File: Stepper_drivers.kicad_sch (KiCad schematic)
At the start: 9 parts, among them J6 ${STEPGEN_CH1_NAME}_STEP_AND_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, J7 ${STEPGEN_CH2_NAME}_STEP_AND_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, U5 ADuM1200AR, U6 ADuM1200AR, U7 HT26LS31ARZ

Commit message: Fixes to screw terminal footprints, updated BOM and included in project folder
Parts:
- J6, J7: footprint OSTVTerminalBlocks:Conn01x06 -> EBWA_06_A:CONN_EBWA-06-A_ADM
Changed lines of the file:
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@@
 				)
 				(path "/5473abc6-7b93-43cc-a401-f691c4d7d7cf/de6abc2f-b4f3-405f-80dc-20e6ec6edfe3"
-					(reference "#PWR0143")
-					(unit 1)
-				)
-				(path "/5473abc6-7b93-43cc-a401-f691c4d7d7cf/ee859447-e27b-4f56-862a-3601314a5b43"
-					(reference "#PWR0143")
+					(reference "#PWR0142")
+					(unit 1)
+				)
+				(path "/5473abc6-7b93-43cc-a401-f691c4d7d7cf/ee859447-e27b-4f56-862a-3601314a5b43"
+					(reference "#PWR0140")
 					(unit 1)
 				)
@@
 			)
 		)
-		(property "Footprint" "OSTVTerminalBlocks:Conn01x06"
+		(property "Footprint" "EBWA_06_A:CONN_EBWA-06-A_ADM"
 			(at 200.66 80.01 0)
 			(effects
@@
 			)
 		)
-		(property "Footprint" "OSTVTerminalBlocks:Conn01x06"
+		(property "Footprint" "EBWA_06_A:CONN_EBWA-06-A_ADM"
 			(at 200.66 105.41 0)
 			(effects

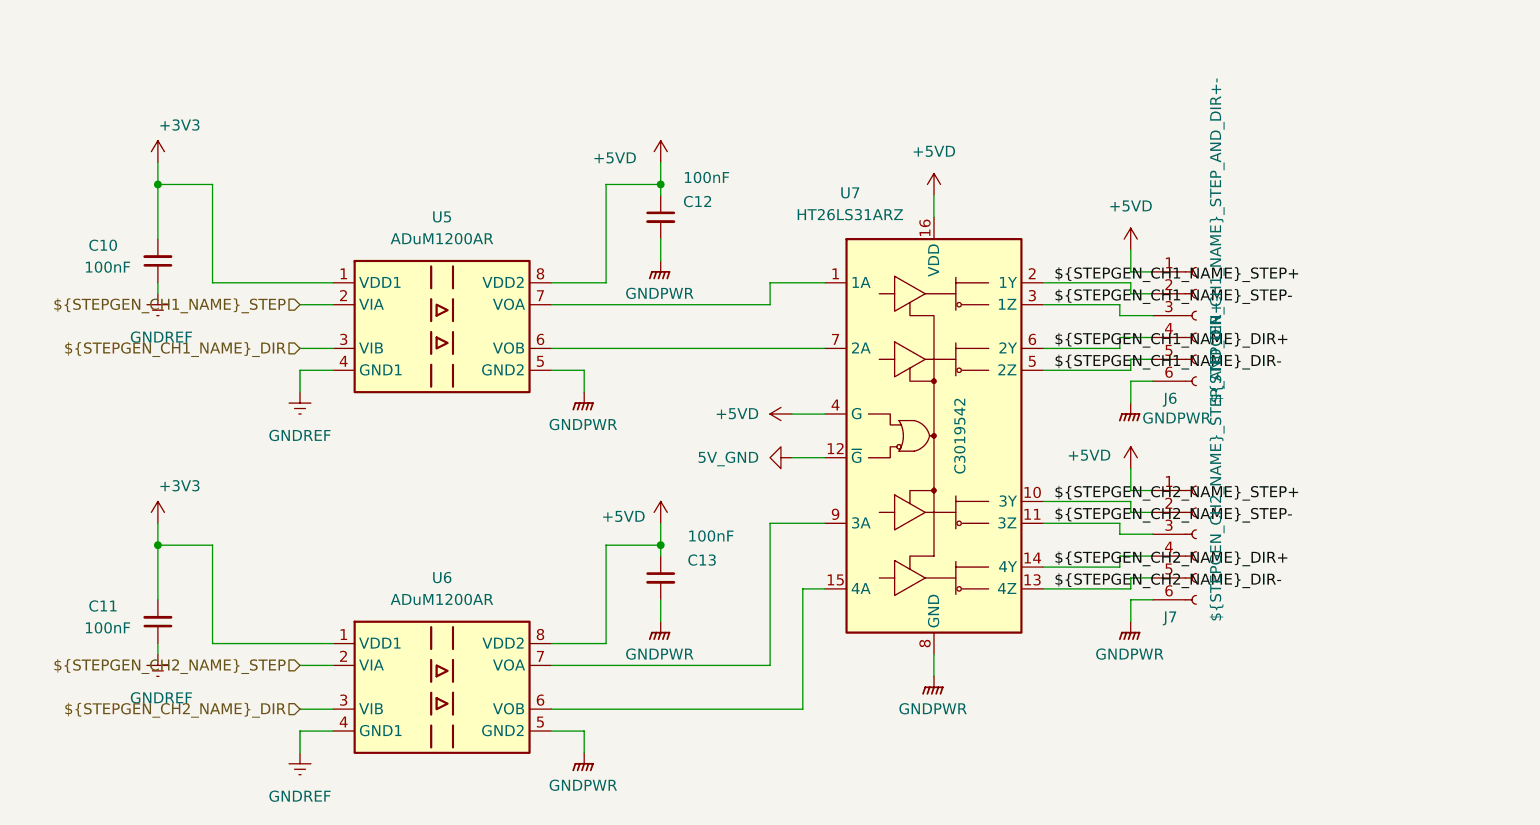
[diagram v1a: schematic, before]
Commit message: updates to read me, marked V1 parts inactive and made start on board layout for initial test board. fixes to BOM to suit
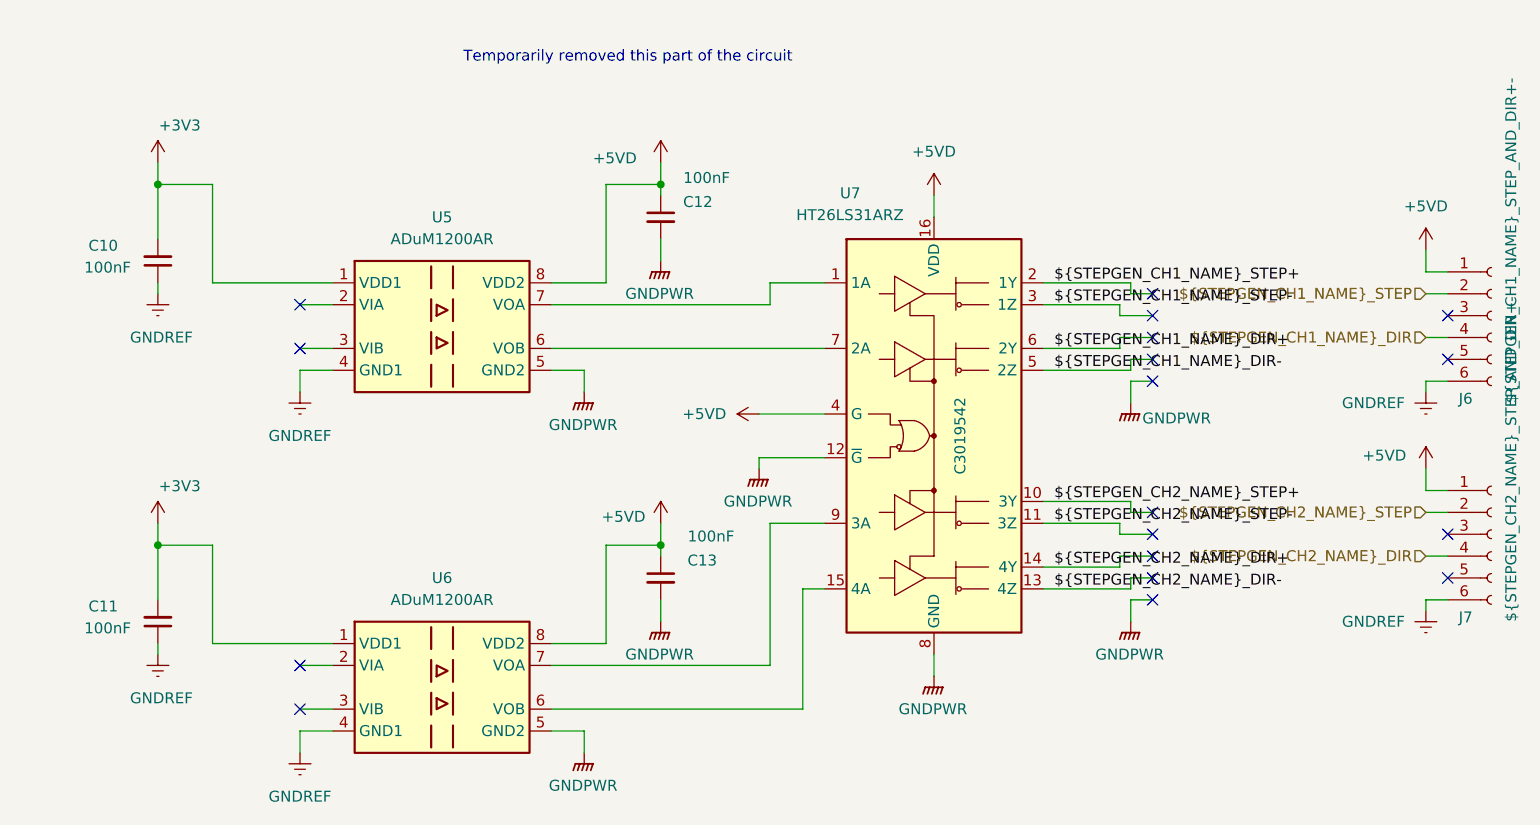
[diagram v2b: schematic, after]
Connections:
- net 5V_GND is gone; now on net GNDPWR: U7.12 (~{G})
- net ${STEPGEN_CH1_NAME}_DIR: now also J6.4 (Pin_4); no longer U5.3 (VIB)
- net ${STEPGEN_CH1_NAME}_DIR+: no longer J6.4 (Pin_4)
- net ${STEPGEN_CH1_NAME}_DIR-: no longer J6.5 (Pin_5)
- net ${STEPGEN_CH1_NAME}_STEP: now also J6.2 (Pin_2); no longer U5.2 (VIA)
- net ${STEPGEN_CH1_NAME}_STEP+: no longer J6.2 (Pin_2)
- net ${STEPGEN_CH1_NAME}_STEP-: no longer J6.3 (Pin_3)
- net ${STEPGEN_CH2_NAME}_DIR: now also J7.4 (Pin_4); no longer U6.3 (VIB)
- net ${STEPGEN_CH2_NAME}_DIR+: no longer J7.4 (Pin_4)
- net ${STEPGEN_CH2_NAME}_DIR-: no longer J7.5 (Pin_5)
- net ${STEPGEN_CH2_NAME}_STEP: now also J7.2 (Pin_2); no longer U6.2 (VIA)
- net ${STEPGEN_CH2_NAME}_STEP+: no longer J7.2 (Pin_2)
- net ${STEPGEN_CH2_NAME}_STEP-: no longer J7.3 (Pin_3)
- net GNDPWR: no longer J6.6 (Pin_6), J7.6 (Pin_6)
- net GNDREF: now also J6.6 (Pin_6), J7.6 (Pin_6)
- no-connect marks 0 -> 18
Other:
- note added: "Temporarily removed this part of the circuit"
- moved on the sheet: J6, J7

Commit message: New optocoupler part choice, removed digikey BOM as have started inputting them into symbol fields. Re-enabled all disabled parts for now and will re-design power supplies soon.
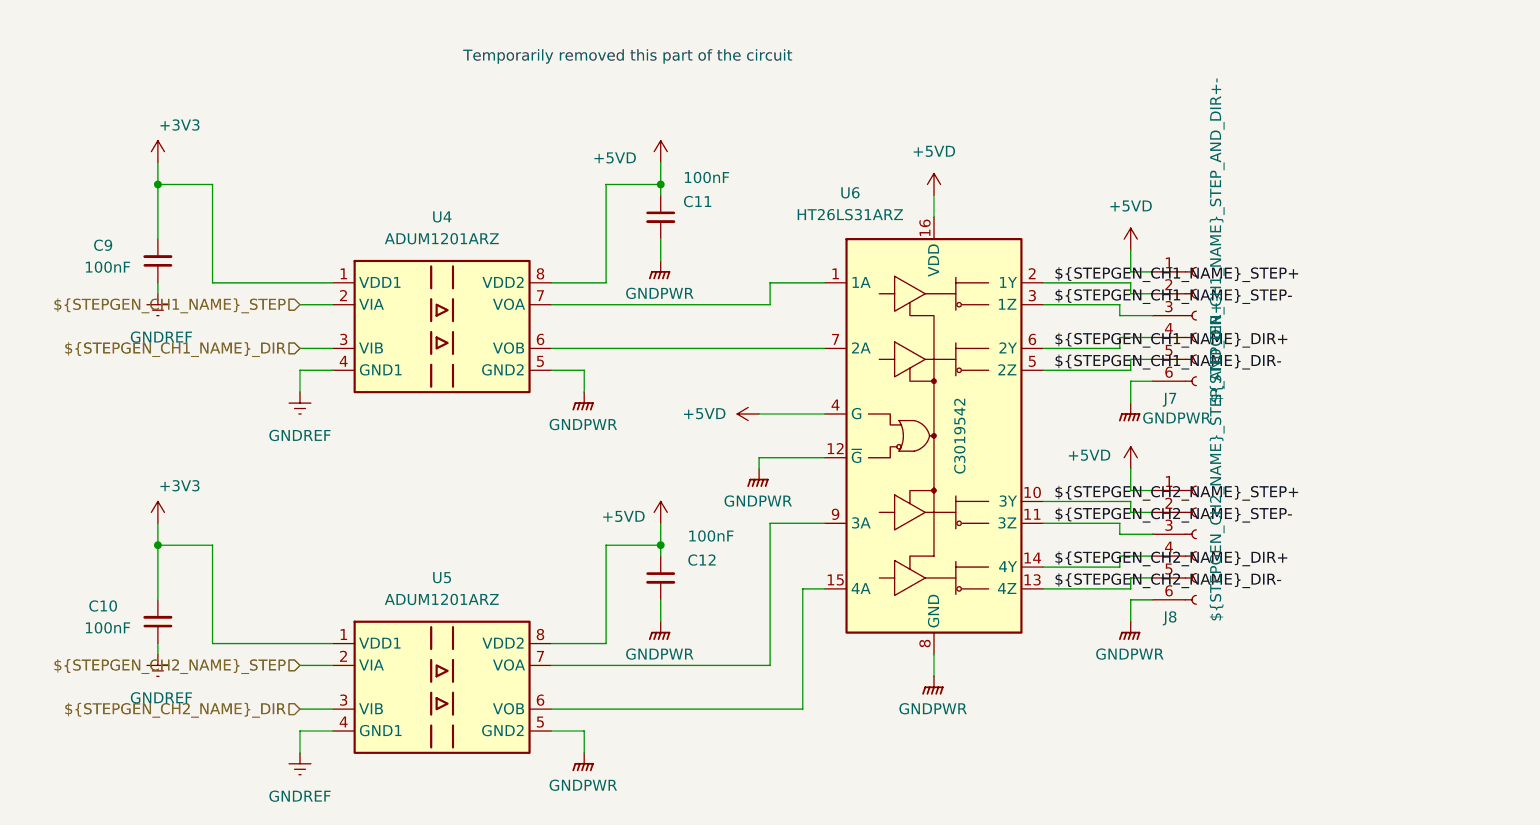
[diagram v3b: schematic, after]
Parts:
- J7: renamed from J6; now in the parts list
- J8: renamed from J7; now in the parts list
- U4: renamed from U5; value ADuM1200AR -> ADUM1201ARZ
- U5: renamed from U6; value ADuM1200AR -> ADUM1201ARZ
- renumbered C11 to C10, C12 to C11, C13 to C12, C10 to C9, U7 to U6
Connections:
- net ${STEPGEN_CH1_NAME}_DIR: now also U4.3 (VIB); no longer J7.4 (Pin_4)
- net ${STEPGEN_CH1_NAME}_DIR+: now also J7.4 (Pin_4)
- net ${STEPGEN_CH1_NAME}_DIR-: now also J7.5 (Pin_5)
- net ${STEPGEN_CH1_NAME}_STEP: now also U4.2 (VIA); no longer J7.2 (Pin_2)
- net ${STEPGEN_CH1_NAME}_STEP+: now also J7.2 (Pin_2)
- net ${STEPGEN_CH1_NAME}_STEP-: now also J7.3 (Pin_3)
- net ${STEPGEN_CH2_NAME}_DIR: now also U5.3 (VIB); no longer J8.4 (Pin_4)
- net ${STEPGEN_CH2_NAME}_DIR+: now also J8.4 (Pin_4)
- net ${STEPGEN_CH2_NAME}_DIR-: now also J8.5 (Pin_5)
- net ${STEPGEN_CH2_NAME}_STEP: now also U5.2 (VIA); no longer J8.2 (Pin_2)
- net ${STEPGEN_CH2_NAME}_STEP+: now also J8.2 (Pin_2)
- net ${STEPGEN_CH2_NAME}_STEP-: now also J8.3 (Pin_3)
- net GNDPWR: now also J7.6 (Pin_6), J8.6 (Pin_6)
- net GNDREF: no longer J7.6 (Pin_6), J8.6 (Pin_6)
- no-connect marks 18 -> 0
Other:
- moved on the sheet: J7, J8

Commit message: fix to annoying additional symbol fields displaying when we didn't want them to.
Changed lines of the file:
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@@
 					(size 1.27 1.27)
 				)
+				(hide yes)
 			)
 		)
@@
 					(size 1.27 1.27)
 				)
+				(hide yes)
 			)
 		)
@@
 					(size 1.27 1.27)
 				)
+				(hide yes)
 			)
 		)
@@
 					(size 1.27 1.27)
 				)
+				(hide yes)
 			)
 		)
@@
 					(size 1.27 1.27)
 				)
+				(hide yes)
 			)
 		)
@@
 					(size 1.27 1.27)
 				)
+				(hide yes)
 			)
 		)
@@
 					(size 1.27 1.27)
 				)
+				(hide yes)
 			)
 		)
@@
 					(size 1.27 1.27)
 				)
+				(hide yes)
 			)
 		)
@@
 					(size 1.27 1.27)
 				)
+				(hide yes)
 			)
 		)
@@
 					(size 1.27 1.27)
 				)
+				(hide yes)
 			)
 		)
@@
 					(size 1.27 1.27)
 				)
+				(hide yes)
 			)
 		)
@@
 					(size 1.27 1.27)
 				)
+				(hide yes)
 			)
 		)
@@
 					(size 1.27 1.27)
 				)
+				(hide yes)
 			)
 		)
@@
 					(size 1.27 1.27)
 				)
+				(hide yes)
 			)
 		)
@@
 					(size 1.27 1.27)
 				)
+				(hide yes)
 			)
 		)
@@
 					(size 1.27 1.27)
 				)
+				(hide yes)
 			)
 		)
@@
 					(size 1.27 1.27)
 				)
+				(hide yes)
 			)
 		)
@@
 					(size 1.27 1.27)
 				)
+				(hide yes)
 			)
 		)
@@
 					(size 1.27 1.27)
 				)
-			)
-		)
+				(hide yes)
+			)
+		)

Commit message: BOM consolidation for various resistors. Moved BOM into symbol libraries and updated supplimentary BOM. Switched IO optical isolation circuitry to a more cost effective part.
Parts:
- J7: Digikey Part Number (none) -> 2057-EBWA-06-A-ND; Digikey URL (none) -> https://www.digikey.com/en/products/detail/adam-tech/EBWA-0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
- J8: Digikey Part Number (none) -> 5239-EK350A-06P-ND; Digikey URL (none) -> https://www.digikey.com.au/en/products/detail/dinkle-corpor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
- U4, U5: Digikey Part Number (none) -> 505-ADUM1201ARZ-RL7CT-ND; Digikey URL (none) -> https://www.digikey.com.au/en/products/detail/analog-device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
- U6: Digikey Part Number (none) -> 296-1010-1-ND; Digikey URL (none) -> https://www.digikey.com.au/en/products/detail/texas-instrum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
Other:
- note removed: "Temporarily removed this part of the circuit"
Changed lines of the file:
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@@
 	(generator_version "9.0")
 	(paper "A4")
-	(text "Temporarily removed this part of the circuit\n"
-		(exclude_from_sim no)
-		(at 134.62 50.038 0)
-		(effects
-			(font
-				(size 1.27 1.27)
-			)
-		)
-	)
 	(junction
 		(at 138.43 106.68)
@@
 			)
 		)
-		(property "Digikey Part Number" ""
+		(property "Digikey Part Number" "505-ADUM1201ARZ-RL7CT-ND"
 			(at 113.03 81.28 0)
 			(effects
@@
 			)
 		)
-		(property "Digikey URL" ""
+		(property "Digikey URL" "https://www.digikey.com.au/en/products/detail/analog-devices-inc/ADUM1201ARZ-RL7/995629"
 			(at 113.03 81.28 0)
 			(effects
@@
 			)
 		)
-		(property "Digikey Part Number" ""
+		(property "Digikey Part Number" "296-1010-1-ND"
 			(at 170.18 93.98 0)
 			(effects
@@
 			)
 		)
-		(property "Digikey URL" ""
+		(property "Digikey URL" "https://www.digikey.com.au/en/products/detail/texas-instruments/AM26LS31CDR/276654"
 			(at 170.18 93.98 0)
 			(effects
@@
 			)
 		)
-		(property "Digikey Part Number" ""
+		(property "Digikey Part Number" "505-ADUM1201ARZ-RL7CT-ND"
 			(at 113.03 123.19 0)
 			(effects
@@
 			)
 		)
-		(property "Digikey URL" ""
+		(property "Digikey URL" "https://www.digikey.com.au/en/products/detail/analog-devices-inc/ADUM1201ARZ-RL7/995629"
 			(at 113.03 123.19 0)
 			(effects
@@
 			)
 		)
-		(property "Digikey Part Number" ""
+		(property "Digikey Part Number" "2057-EBWA-06-A-ND "
 			(at 200.66 80.01 0)
 			(effects
@@
 			)
 		)
-		(property "Digikey URL" ""
+		(property "Digikey URL" "https://www.digikey.com/en/products/detail/adam-tech/EBWA-06-A/9830532 "
 			(at 200.66 80.01 0)
 			(effects
@@
 			)
 		)
-		(property "Digikey Part Number" ""
+		(property "Digikey Part Number" "5239-EK350A-06P-ND "
 			(at 200.66 105.41 0)
 			(effects
@@
 			)
 		)
-		(property "Digikey URL" ""
+		(property "Digikey URL" "https://www.digikey.com.au/en/products/detail/dinkle-corporation-usa/EK350A-06P/25601688 "
 			(at 200.66 105.41 0)
 			(effects

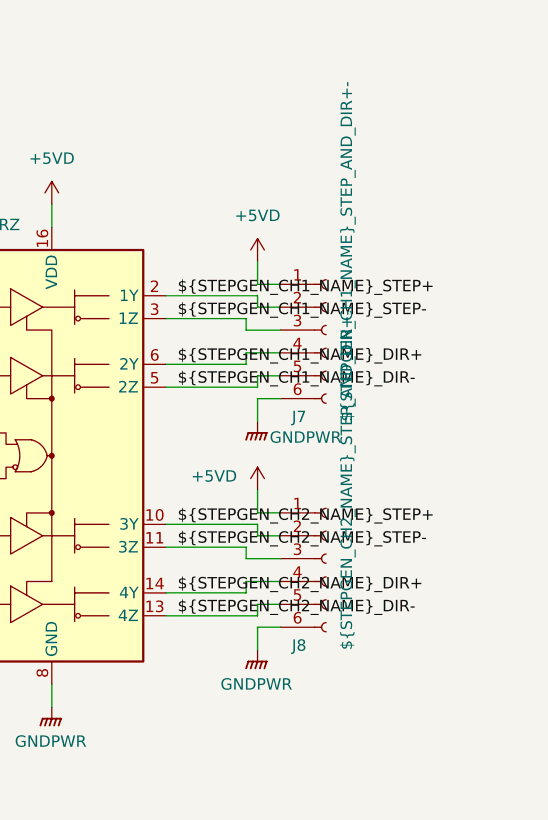
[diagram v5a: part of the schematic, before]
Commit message: more BOM consolidation. Switched out IO for vertical toolless wire to board terminals and added footprints. Put new isolated ground plane on board.
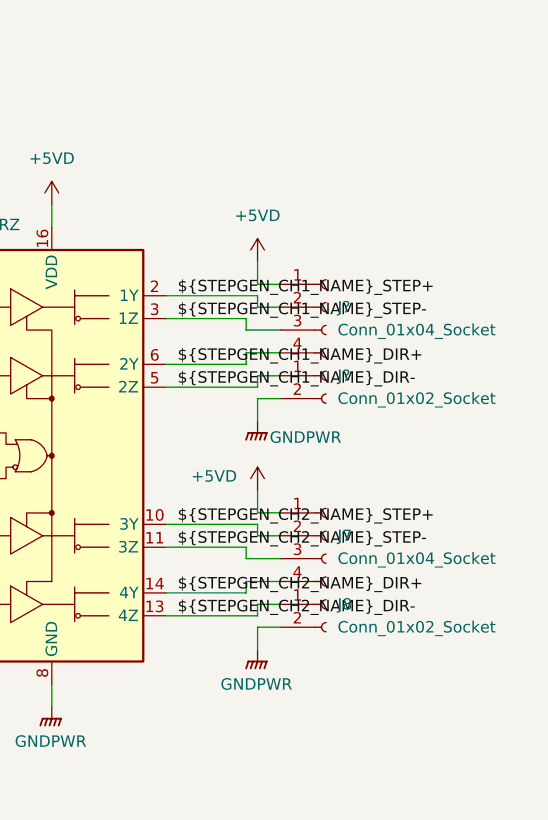
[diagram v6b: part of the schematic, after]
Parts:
- removed J7: ${STEPGEN_CH1_NAME}_STEP_AND_DIR+-, EBWA_06_A:CONN_EBWA-06-A_ADM, symbol Connector:Conn_01x06_Socket
- removed J8: ${STEPGEN_CH2_NAME}_STEP_AND_DIR+-, EBWA_06_A:CONN_EBWA-06-A_ADM, symbol Connector:Conn_01x06_Socket
- added J7, J?: Conn_01x04_Socket, Amphenol QT:QT04ADP83V0000G, symbol Connector:Conn_01x04_Socket
- added J8, J?: Conn_01x02_Socket, Amphenol QT:QT02ADP83V0000G, symbol Connector:Conn_01x02_Socket
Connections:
- net ${STEPGEN_CH1_NAME}_DIR+: now also J?.4 (Pin_4)
- net ${STEPGEN_CH1_NAME}_DIR-: now also J?.1 (Pin_1)
- net ${STEPGEN_CH1_NAME}_STEP+: now also J?.2 (Pin_2)
- net ${STEPGEN_CH1_NAME}_STEP-: now also J?.3 (Pin_3)
- net ${STEPGEN_CH2_NAME}_DIR+: now also J7.4 (Pin_4)
- net ${STEPGEN_CH2_NAME}_DIR-: now also J8.1 (Pin_1)
- net ${STEPGEN_CH2_NAME}_STEP+: now also J7.2 (Pin_2)
- net ${STEPGEN_CH2_NAME}_STEP-: now also J7.3 (Pin_3)
- net +5VD: now also J7.1 (Pin_1), J?.1 (Pin_1)
- net GNDPWR: now also J8.2 (Pin_2), J?.2 (Pin_2)
